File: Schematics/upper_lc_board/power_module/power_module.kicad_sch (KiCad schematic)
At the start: 25 parts

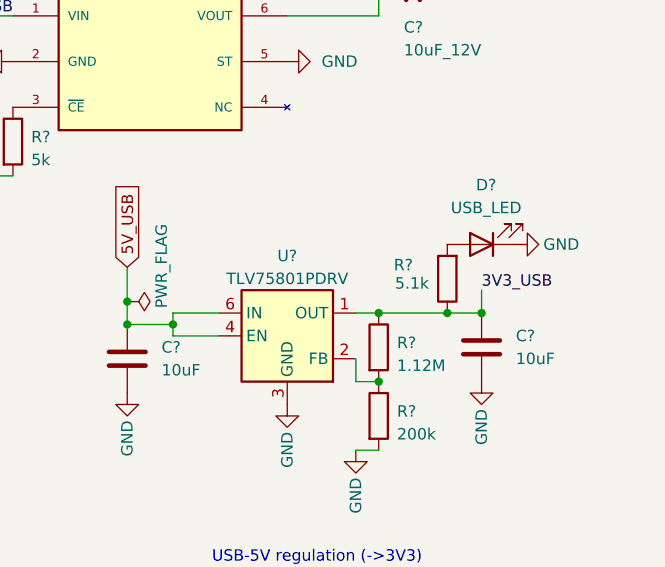
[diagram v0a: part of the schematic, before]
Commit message: update layout with new connector
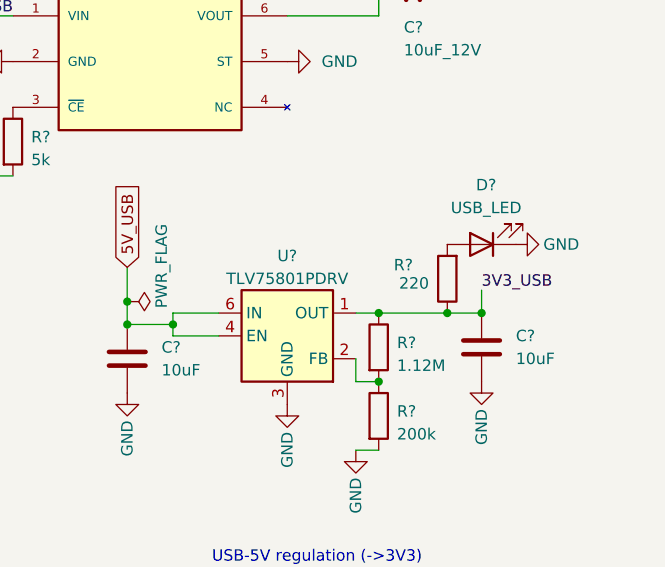
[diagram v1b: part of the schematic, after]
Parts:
- R?: value 5.1k -> 220
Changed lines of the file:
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@@
 			)
 		)
-		(property "Value" "5.1k"
+		(property "Value" "220"
 			(at 193.548 114.808 0)
 			(effects

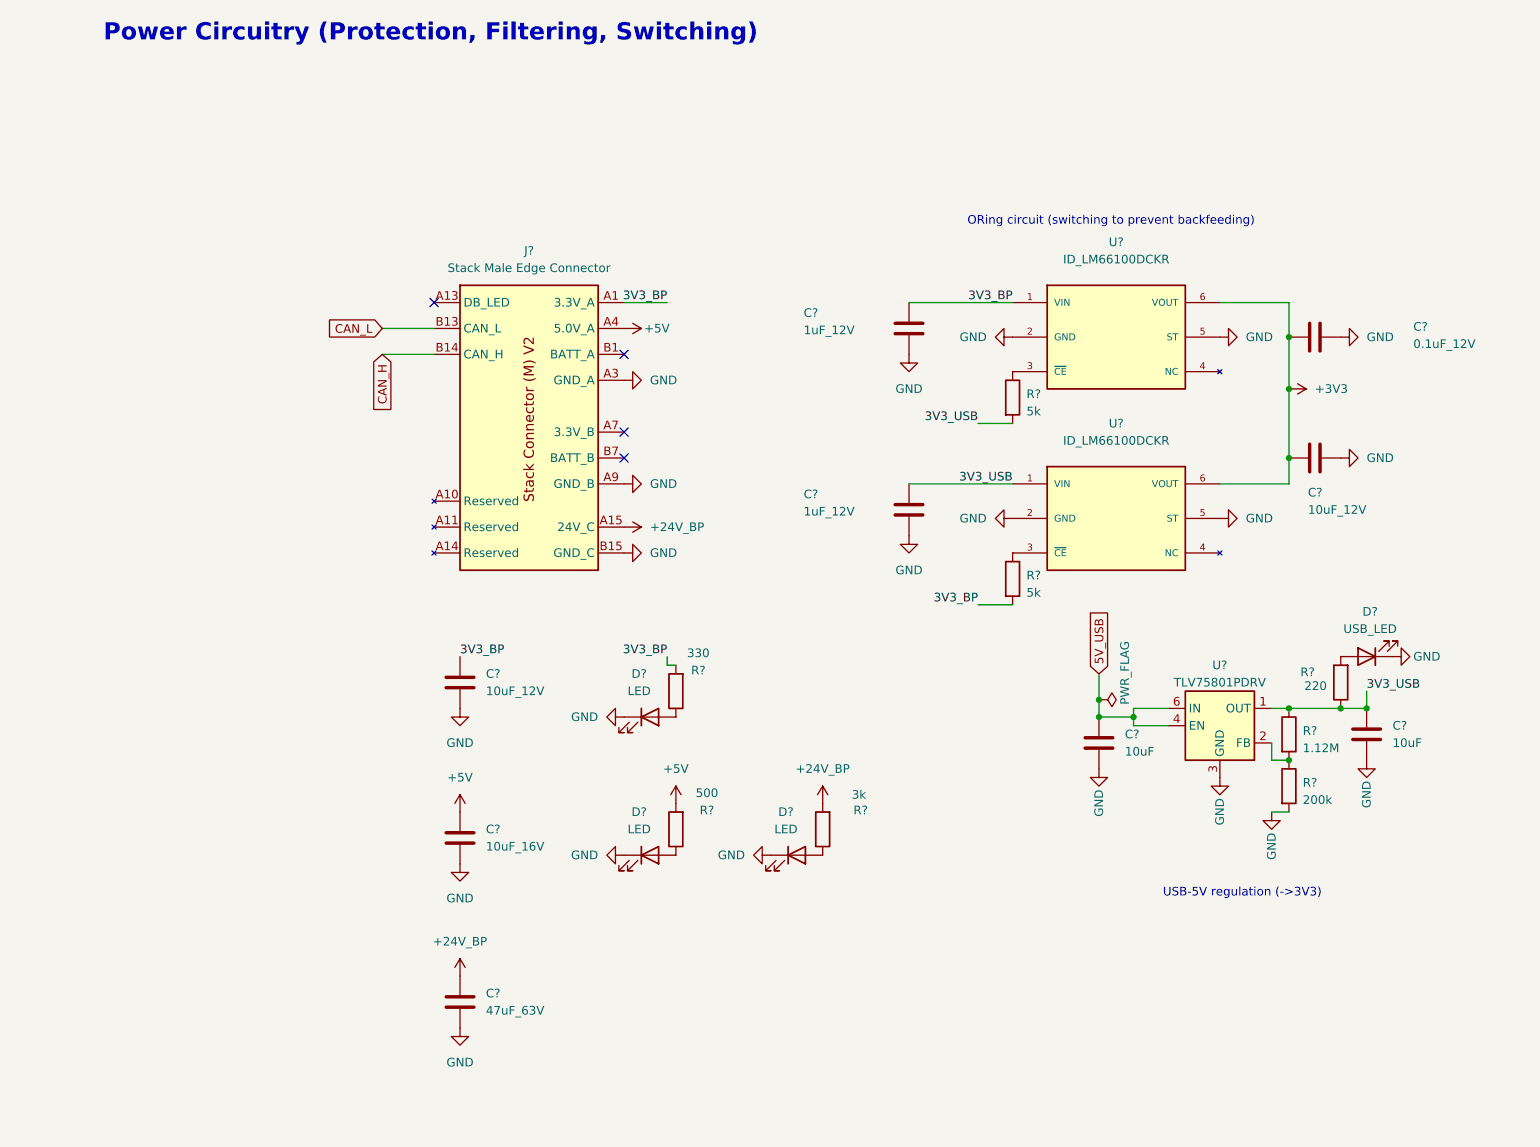
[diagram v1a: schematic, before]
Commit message: start redesigning ADC circuitry, organize schematic files. adding OPAMPS for buffered voltage divider on HALL & on PTs. layout to be adjusted after.
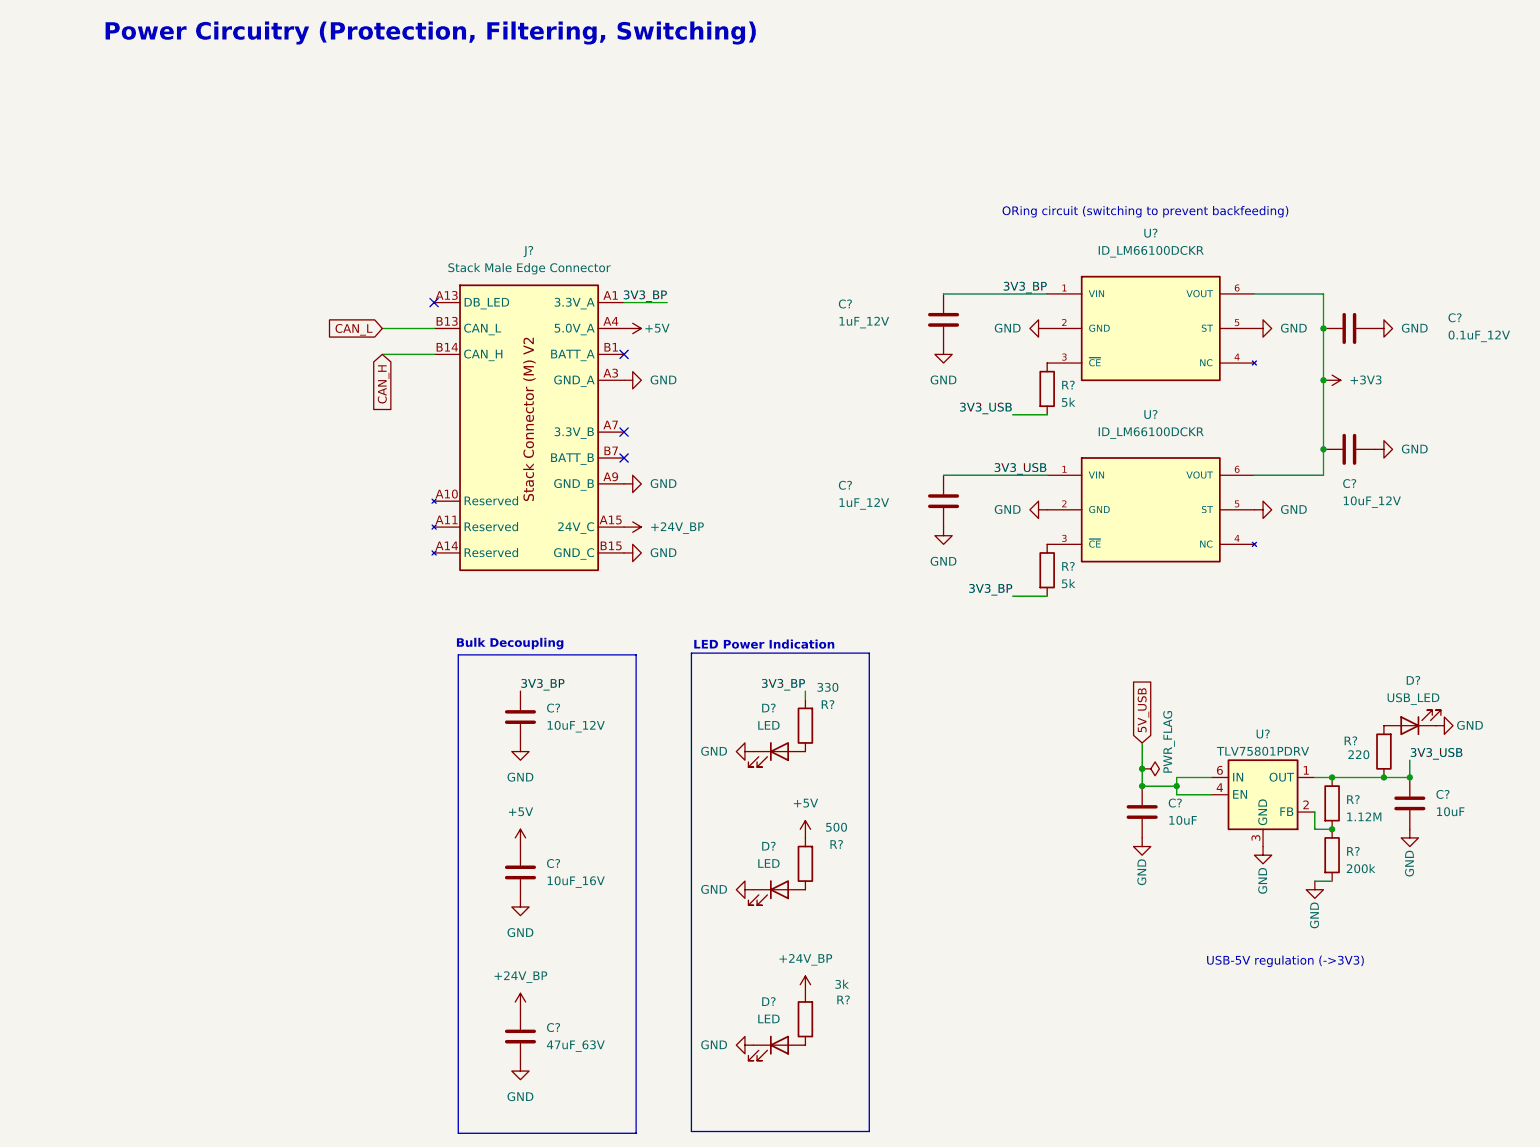
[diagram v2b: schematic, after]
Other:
- note added: "Bulk Decoupling"
- note added: "LED Power Indication"
- moved on the sheet: C?, D?, R?, U?

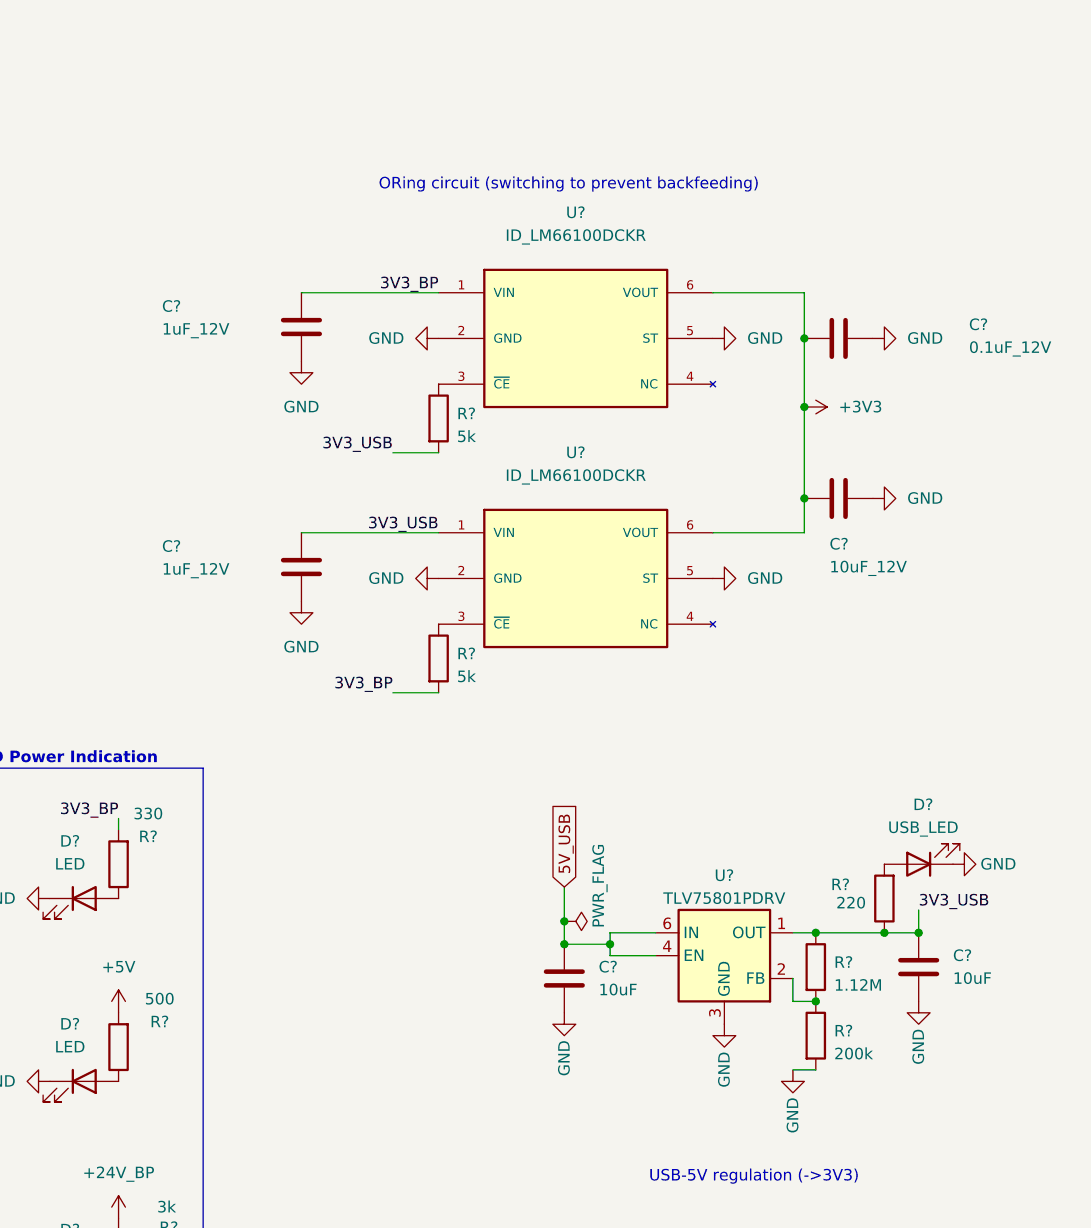
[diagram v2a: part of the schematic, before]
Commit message: solenoid schematic review, reveiewing sensors and ESP-breakout next, then finalizing layout
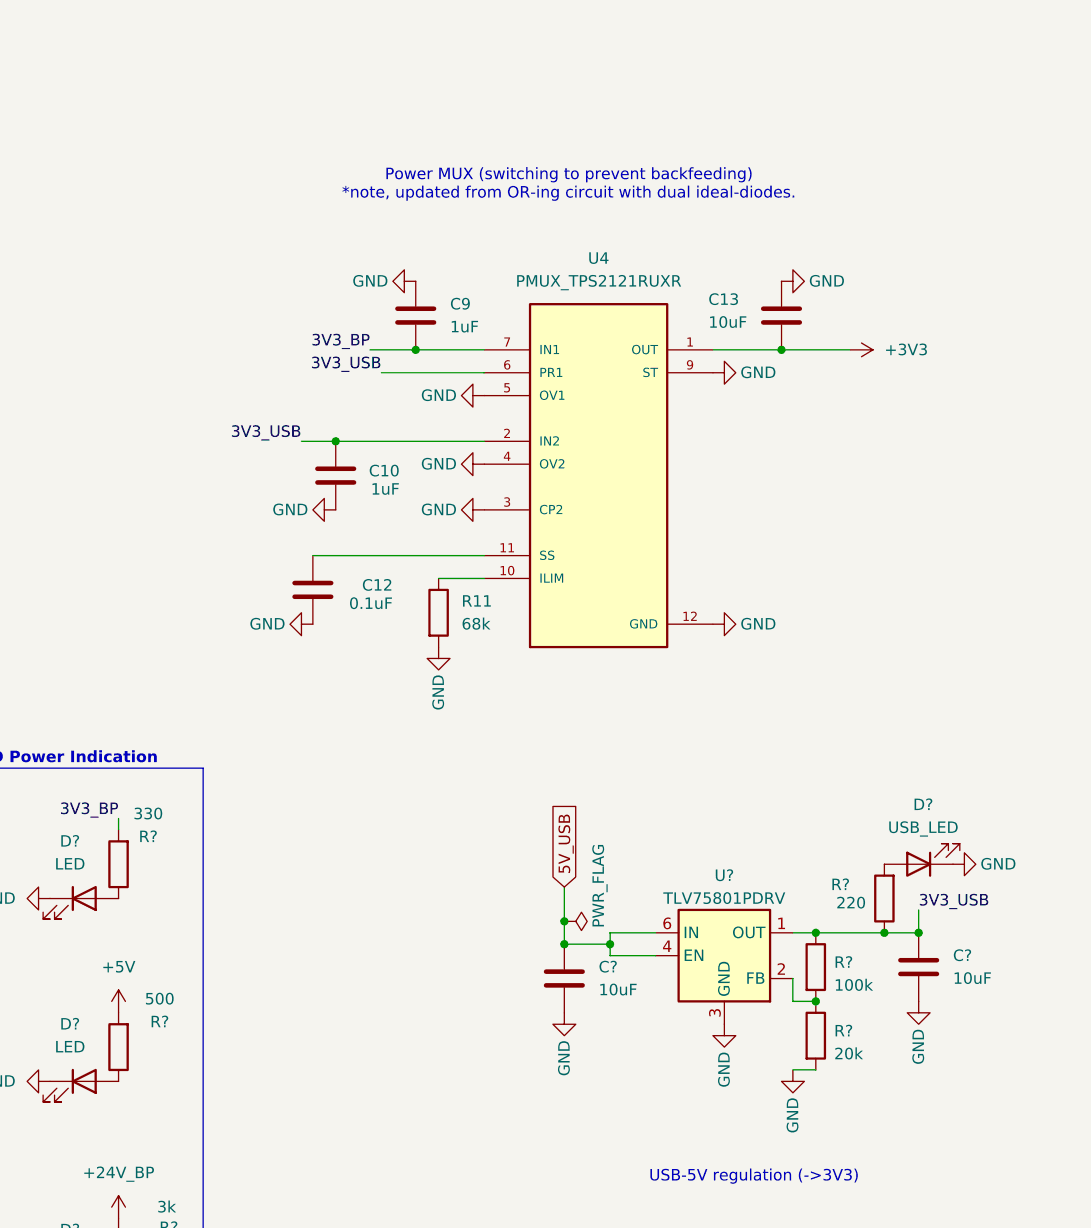
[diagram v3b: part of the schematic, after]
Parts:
- removed C?: 10uF_12V, Capacitor_SMD:C_0603_1608Metric, symbol Device:C
- removed C? (x2): 1uF_12V, Capacitor_SMD:C_0603_1608Metric, symbol Device:C
- removed C?: 0.1uF_12V, Capacitor_SMD:C_0603_1608Metric, symbol Device:C
- removed R? (x2): 5k, Capacitor_SMD:C_0402_1005Metric, symbol Device:R
- removed U? (x2): ID_LM66100DCKR, LM66100DCKR:SOT65P210X110-6N, symbol LM66100DCKR:LM66100DCKR
- added C10, C9: 1uF, symbol Device:C
- added C12: 0.1uF, symbol Device:C
- added C13: 10uF, symbol Device:C
- added R11: 68k, symbol Device:R
- added U4: PMUX_TPS2121RUXR, TPS2121RUXR:IC_TPS2121RUXR, symbol TPS2121RUXR:TPS2121RUXR
- R?: value 200k -> 20k
- R?: value 1.12M -> 100k
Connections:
- net +3V3: now also C13.2, U4.1 (OUT), U4.1_1 (OUT), U4.8 (OUT), U4.8_1 (OUT)
- net 3V3_BP: now also C9.2, U4.7 (IN1), U4.7_1 (IN1)
- net 3V3_USB: now also C10.2, U4.2 (IN2), U4.2_1 (IN2), U4.6 (PR1)
- net GND: now also C10.1, C12.1, C13.1, C9.1, R11.2, U4.12 (GND), U4.3 (CP2), U4.4 (OV2), U4.5 (OV1), U4.9 (ST)
- new net: R11.1, U4.10 (ILIM)
- new net: C12.2, U4.11 (SS)
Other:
- note added: "Power MUX (switching to prevent backfeeding) *note, updated from OR-ing circuit with dual ideal-diodes."
- note removed: "ORing circuit (switching to prevent backfeeding)"

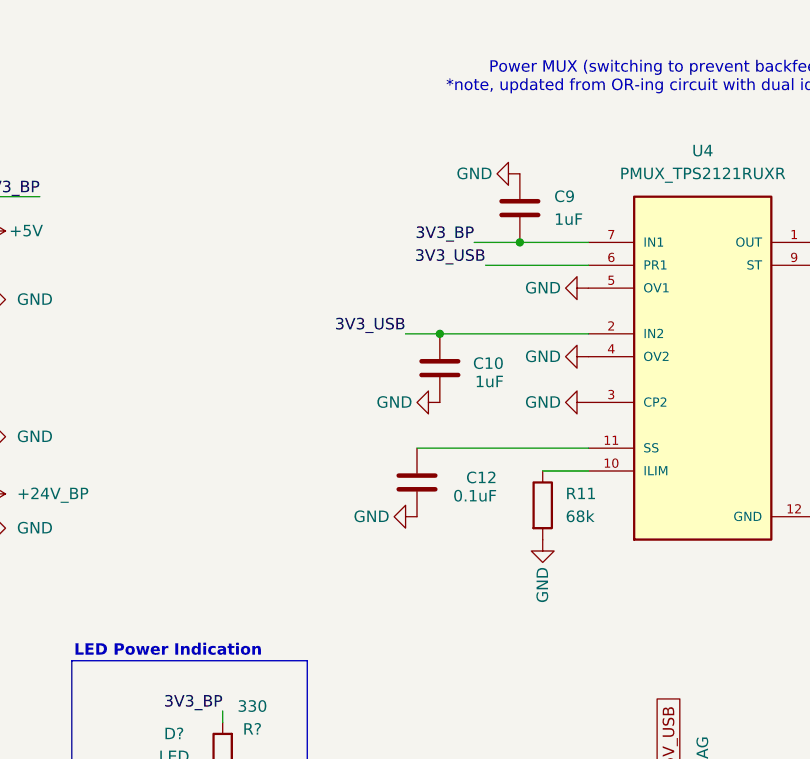
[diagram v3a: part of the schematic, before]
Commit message: finish power circuitry (MUX)
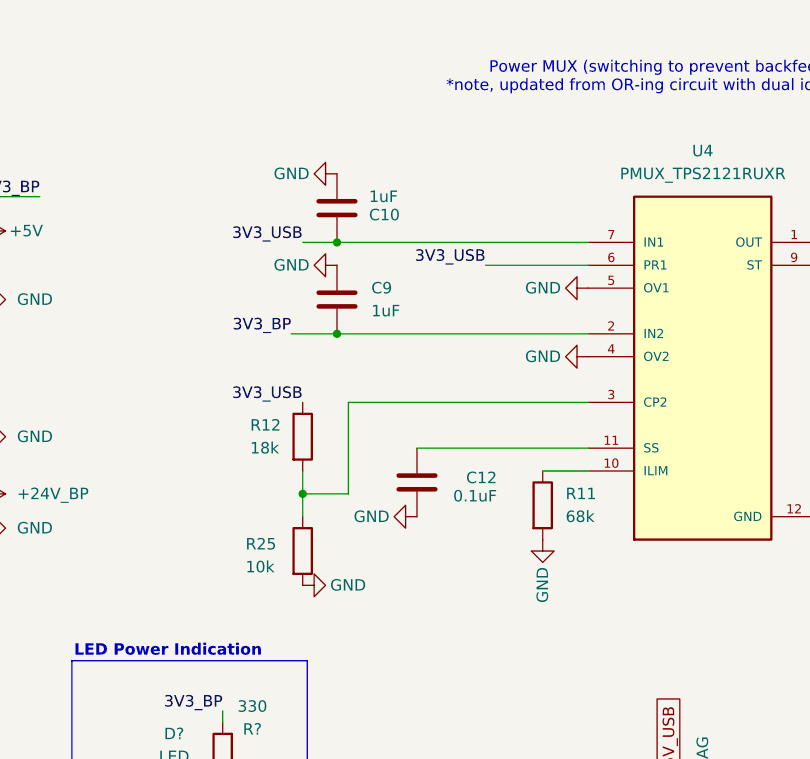
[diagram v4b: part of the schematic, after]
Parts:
- added R12: 18k, symbol Device:R
- added R25: 10k, symbol Device:R
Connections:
- net 3V3_BP: now also U4.2 (IN2), U4.2_1 (IN2); no longer U4.7 (IN1), U4.7_1 (IN1)
- net 3V3_USB: now also U4.7 (IN1), U4.7_1 (IN1), R12.1; no longer U4.2 (IN2), U4.2_1 (IN2)
- net GND: now also R25.2; no longer U4.3 (CP2)
- new net: R12.2, R25.1, U4.3 (CP2)
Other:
- moved on the sheet: C10

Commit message: breakout circuitry review
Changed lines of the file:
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@@
 	)
 	(junction
+		(at 90.17 58.42)
+		(diameter 0)
+		(color 194 0 0 1)
+	)
+	(junction
 		(at 166.37 127)
 		(diameter 0)
@@
 	(wire
 		(pts
-			(xy 90.17 58.42) (xy 96.52 58.42)
+			(xy 90.17 58.42) (xy 101.6 58.42)
 		)
 		(stroke
@@
 	(wire
 		(pts
+			(xy 90.17 58.42) (xy 90.17 54.61)
+		)
+		(stroke
+			(width 0)
+			(type default)
+			(color 194 0 0 1)
+		)
+	)
+	(wire
+		(pts
 			(xy 125.73 88.9) (xy 125.73 91.44)
 		)
@@
 	(wire
 		(pts
+			(xy 90.17 54.61) (xy 100.33 54.61)
+		)
+		(stroke
+			(width 0)
+			(type default)
+			(color 194 0 0 1)
+		)
+	)
+	(wire
+		(pts
 			(xy 191.77 128.27) (xy 194.31 128.27)
 		)
@@
 	(wire
 		(pts
+			(xy 205.74 125.73) (xy 215.9 125.73)
+		)
+		(stroke
+			(width 0)
+			(type default)
+		)
+	)
+	(wire
+		(pts
 			(xy 124.46 73.66) (xy 129.54 73.66)
 		)
@@
 	)
 	(label "3V3_BP"
-		(at 96.52 58.42 180)
+		(at 101.6 58.42 180)
 		(fields_autoplaced yes)
 		(effects
@@
 	)
 	(symbol
+		(lib_id "power:PWR_FLAG")
+		(at 100.33 54.61 270)
+		(unit 1)
+		(exclude_from_sim no)
+		(in_bom yes)
+		(on_board yes)
+		(dnp no)
+		(property "Reference" "#FLG03"
+			(at 102.235 54.61 0)
+			(effects
+				(font
+					(size 1.27 1.27)
+				)
+				(hide yes)
+			)
+		)
+		(property "Value" "PWR_FLAG"
+			(at 104.14 45.974 0)
+			(effects
+				(font
+					(size 1.27 1.27)
+				)
+				(justify left)
+			)
+		)
+		(property "Footprint" ""
+			(at 100.33 54.61 0)
+			(effects
+				(font
+					(size 1.27 1.27)
+				)
+				(hide yes)
+			)
+		)
+		(property "Datasheet" "~"
+			(at 100.33 54.61 0)
+			(effects
+				(font
+					(size 1.27 1.27)
+				)
+				(hide yes)
+			)
+		)
+		(property "Description" "Special symbol for telling ERC where power comes from"
+			(at 100.33 54.61 0)
+			(effects
+				(font
+					(size 1.27 1.27)
+				)
+				(hide yes)
+			)
+		)
+		(pin "1"
+		)
+		(instances
+			(project "upper_lc_board"
+				(path "/9b1a1d2a-fad7-4f10-83f3-1f83e9656c75/4448a9b0-3cba-4e30-89c0-980036e20f76"
+					(reference "#FLG03")
+					(unit 1)
+				)
+			)
+		)
+	)
+	(symbol
 		(lib_id "Device:R")
 		(at 194.31 139.7 0)
@@
 					(unit 1)
 				)
+			)
+		)
+	)
+	(symbol
+		(lib_id "power:PWR_FLAG")
+		(at 215.9 125.73 270)
+		(unit 1)
+		(exclude_from_sim no)
+		(in_bom yes)
+		(on_board yes)
+		(dnp no)
+		(property "Reference" "#FLG02"
+			(at 217.805 125.73 0)
+			(effects
+				(font
+					(size 1.27 1.27)
+				)
+				(hide yes)
+			)
+		)
+		(property "Value" "PWR_FLAG"
+			(at 219.71 117.094 0)
+			(effects
+				(font
+					(size 1.27 1.27)
+				)
+				(justify left)
+			)
+		)
+		(property "Footprint" ""
+			(at 215.9 125.73 0)
+			(effects
+				(font
+					(size 1.27 1.27)
+				)
+				(hide yes)
+			)
+		)
+		(property "Datasheet" "~"
+			(at 215.9 125.73 0)
+			(effects
+				(font
+					(size 1.27 1.27)
+				)
+				(hide yes)
+			)
+		)
+		(property "Description" "Special symbol for telling ERC where power comes from"
+			(at 215.9 125.73 0)
+			(effects
+				(font
+					(size 1.27 1.27)
+				)
+				(hide yes)
+			)
+		)
+		(pin "1"
+		)
+		(instances
+			(project "upper_lc_board"
+				(path "/9b1a1d2a-fad7-4f10-83f3-1f83e9656c75/4448a9b0-3cba-4e30-89c0-980036e20f76"
+					(reference "#FLG02")
+					(unit 1)
+				)
